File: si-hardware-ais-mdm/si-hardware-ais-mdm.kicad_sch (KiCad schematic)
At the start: 0 parts

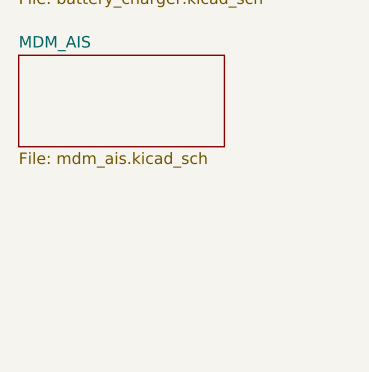
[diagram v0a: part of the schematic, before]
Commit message: added function power input battery chargger mdm_ais
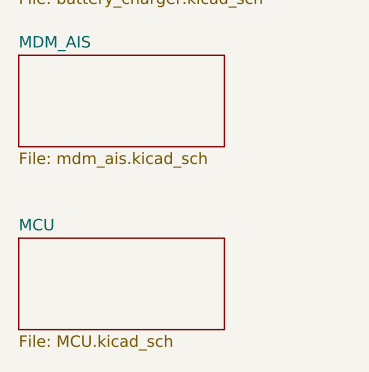
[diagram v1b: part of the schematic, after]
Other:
- added sheet MCU (MCU.kicad_sch)
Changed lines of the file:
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@@
+	)
+	(sheet
+		(at 138.43 132.08)
+		(size 22.86 10.16)
+		(fields_autoplaced yes)
+		(stroke
+			(width 0.1524)
+			(type solid)
+		)
+		(fill
+			(color 0 0 0 0.0000)
+		)
+		(property "Sheetname" "MCU"
+			(at 138.43 131.3684 0)
+			(effects
+				(font
+					(size 1.27 1.27)
+				)
+				(justify left bottom)
+			)
+		)
+		(property "Sheetfile" "MCU.kicad_sch"
+			(at 138.43 142.8246 0)
+			(effects
+				(font
+					(size 1.27 1.27)
+				)
+				(justify left top)
+			)
+		)
+		(instances
+			(project "si-hardware-ais-mdm"
+				(path "/97f80214-d5cc-4a35-9cac-bb1ff8330c6a"
+					(page "5")
+				)
+			)
+		)
 	)
 	(sheet

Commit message: schematic  to pcb
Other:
- sheet BATTERY_CHARGER ports: added V_BUS; removed none
- sheet MCU ports: added +3.3V, V_BUS, mdm_ais; removed none
- sheet MDM_AIS ports: added +3.3V, mdm_ais; removed none
- sheet POWER_INPUT ports: added +3.3V, V_BUS; removed none
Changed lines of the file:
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@@
 	(generator_version "8.0")
 	(paper "A4")
+	(junction
+		(at 109.22 82.55)
+		(diameter 0)
+		(color 0 0 0 0)
+	)
+	(wire
+		(pts
+			(xy 105.41 82.55) (xy 109.22 82.55)
+		)
+		(stroke
+			(width 0)
+			(type default)
+		)
+	)
+	(wire
+		(pts
+			(xy 111.76 106.68) (xy 111.76 102.87)
+		)
+		(stroke
+			(width 0)
+			(type default)
+		)
+	)
+	(wire
+		(pts
+			(xy 105.41 97.79) (xy 109.22 97.79)
+		)
+		(stroke
+			(width 0)
+			(type default)
+		)
+	)
+	(wire
+		(pts
+			(xy 109.22 82.55) (xy 115.57 82.55)
+		)
+		(stroke
+			(width 0)
+			(type default)
+		)
+	)
+	(wire
+		(pts
+			(xy 115.57 97.79) (xy 110.49 97.79)
+		)
+		(stroke
+			(width 0)
+			(type default)
+		)
+	)
+	(wire
+		(pts
+			(xy 111.76 102.87) (xy 115.57 102.87)
+		)
+		(stroke
+			(width 0)
+			(type default)
+		)
+	)
+	(wire
+		(pts
+			(xy 105.41 106.68) (xy 111.76 106.68)
+		)
+		(stroke
+			(width 0)
+			(type default)
+		)
+	)
+	(wire
+		(pts
+			(xy 110.49 101.6) (xy 105.41 101.6)
+		)
+		(stroke
+			(width 0)
+			(type default)
+		)
+	)
+	(wire
+		(pts
+			(xy 110.49 97.79) (xy 110.49 101.6)
+		)
+		(stroke
+			(width 0)
+			(type default)
+		)
+	)
+	(wire
+		(pts
+			(xy 109.22 97.79) (xy 109.22 82.55)
+		)
+		(stroke
+			(width 0)
+			(type default)
+		)
+	)
 	(sheet
-		(at 138.43 80.01)
-		(size 22.86 7.62)
+		(at 115.57 80.01)
+		(size 22.86 8.89)
 		(fields_autoplaced yes)
 		(stroke
@@
 		)
 		(property "Sheetname" "POWER_INPUT"
-			(at 138.43 79.2984 0)
+			(at 115.57 79.2984 0)
 			(effects
 				(font
@@
 		)
 		(property "Sheetfile" "power_input.kicad_sch"
-			(at 138.43 88.2146 0)
+			(at 115.57 89.4846 0)
 			(effects
 				(font
@@
 				)
 				(justify left top)
+			)
+		)
+		(pin "V_BUS" input
+			(at 115.57 82.55 180)
+			(effects
+				(font
+					(size 1.27 1.27)
+				)
+				(justify left)
+			)
+		)
+		(pin "+3.3V" input
+			(at 115.57 86.36 180)
+			(effects
+				(font
+					(size 1.27 1.27)
+				)
+				(justify left)
 			)
 		)
@@
 	)
 	(sheet
-		(at 138.43 132.08)
-		(size 22.86 10.16)
+		(at 82.55 95.25)
+		(size 22.86 13.97)
 		(fields_autoplaced yes)
 		(stroke
@@
 		)
 		(property "Sheetname" "MCU"
-			(at 138.43 131.3684 0)
+			(at 82.55 94.5384 0)
 			(effects
 				(font
@@
 		)
 		(property "Sheetfile" "MCU.kicad_sch"
-			(at 138.43 142.8246 0)
+			(at 82.55 109.8046 0)
 			(effects
 				(font
@@
 				)
 				(justify left top)
+			)
+		)
+		(pin "V_BUS" input
+			(at 105.41 97.79 0)
+			(effects
+				(font
+					(size 1.27 1.27)
+				)
+				(justify right)
+			)
+		)
+		(pin "mdm_ais" input
+			(at 105.41 106.68 0)
+			(effects
+				(font
+					(size 1.27 1.27)
+				)
+				(justify right)
+			)
+		)
+		(pin "+3.3V" input
+			(at 105.41 101.6 0)
+			(effects
+				(font
+					(size 1.27 1.27)
+				)
+				(justify right)
 			)
 		)
@@
 	)
 	(sheet
-		(at 138.43 111.76)
-		(size 22.86 10.16)
+		(at 115.57 95.25)
+		(size 22.86 13.97)
 		(fields_autoplaced yes)
 		(stroke
@@
 		)
 		(property "Sheetname" "MDM_AIS"
-			(at 138.43 111.0484 0)
+			(at 115.57 94.5384 0)
 			(effects
 				(font
@@
 		)
 		(property "Sheetfile" "mdm_ais.kicad_sch"
-			(at 138.43 122.5046 0)
+			(at 115.57 109.8046 0)
 			(effects
 				(font
@@
 				)
 				(justify left top)
+			)
+		)
+		(pin "mdm_ais" input
+			(at 115.57 102.87 180)
+			(effects
+				(font
+					(size 1.27 1.27)
+				)
+				(justify left)
+			)
+		)
+		(pin "+3.3V" input
+			(at 115.57 97.79 180)
+			(effects
+				(font
+					(size 1.27 1.27)
+				)
+				(justify left)
 			)
 		)
@@
 	)
 	(sheet
-		(at 138.43 96.52)
-		(size 22.86 7.62)
+		(at 82.55 80.01)
+		(size 22.86 8.89)
 		(fields_autoplaced yes)
 		(stroke
@@
 		)
 		(property "Sheetname" "BATTERY_CHARGER"
-			(at 138.43 95.8084 0)
+			(at 82.55 79.2984 0)
 			(effects
 				(font
@@
 		)
 		(property "Sheetfile" "battery_charger.kicad_sch"
-			(at 138.43 104.7246 0)
+			(at 82.55 89.4846 0)
 			(effects
 				(font
@@
 			)
 		)
+		(pin "V_BUS" input
+			(at 105.41 82.55 0)
+			(effects
+				(font
+					(size 1.27 1.27)
+				)
+				(justify right)
+			)
+		)

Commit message: added schematic pdf
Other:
- added sheet PERIPHERAL (peripheral.kicad_sch)
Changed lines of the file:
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@@
+	)
+	(sheet
+		(at 115.316 123.698)
+		(size 23.368 10.668)
+		(fields_autoplaced yes)
+		(stroke
+			(width 0.1524)
+			(type solid)
+		)
+		(fill
+			(color 0 0 0 0.0000)
+		)
+		(property "Sheetname" "PERIPHERAL"
+			(at 115.316 122.9864 0)
+			(effects
+				(font
+					(size 1.27 1.27)
+				)
+				(justify left bottom)
+			)
+		)
+		(property "Sheetfile" "peripheral.kicad_sch"
+			(at 115.316 134.9506 0)
+			(effects
+				(font
+					(size 1.27 1.27)
+				)
+				(justify left top)
+			)
+		)
+		(instances
+			(project "si-hardware-ais-mdm"
+				(path "/97f80214-d5cc-4a35-9cac-bb1ff8330c6a"
+					(page "6")
+				)
+			)
+		)
 	)
 	(sheet
